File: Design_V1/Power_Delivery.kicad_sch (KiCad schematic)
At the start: 1 part

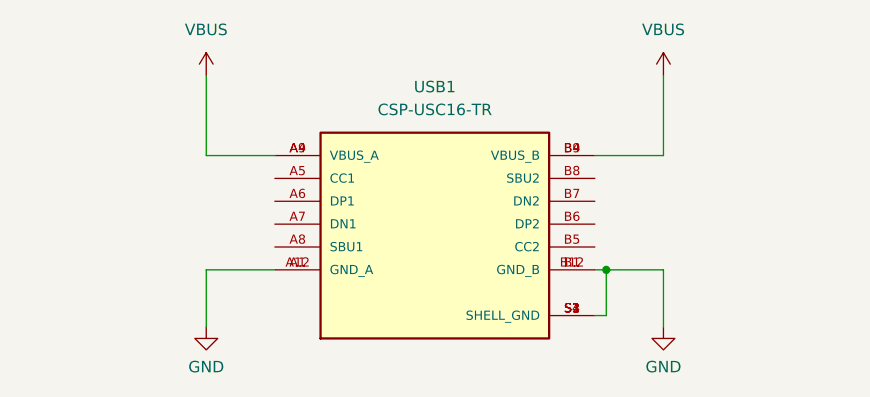
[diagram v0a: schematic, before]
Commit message: Updated Project. Added testpoints, crystal and jumpers. Added Power block
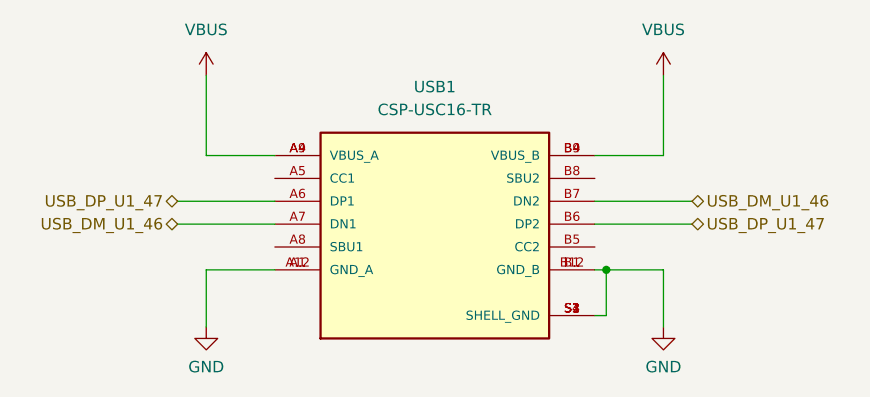
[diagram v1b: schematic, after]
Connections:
- net USB_DP_U1_47: now reaches USB1.A6 (DP1)
- net USB_DP_U1_47: now also USB1.B6 (DP2)
- net USB_DM_U1_46: now reaches USB1.A7 (DN1)
- net USB_DM_U1_46: now also USB1.B7 (DN2)
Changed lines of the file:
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@@
+    (stroke (width 0) (type default) (color 0 0 0 0))
+  )
+  (wire (pts (xy 246.38 110.49) (xy 257.175 110.49))
     (stroke (width 0) (type default) (color 0 0 0 0))
   )
   (wire (pts (xy 254 102.87) (xy 254 93.98))
+    (stroke (width 0) (type default) (color 0 0 0 0))
+  )
+  (wire (pts (xy 210.82 107.95) (xy 200.025 107.95))
+    (stroke (width 0) (type default) (color 0 0 0 0))
+  )
+  (wire (pts (xy 210.82 110.49) (xy 200.025 110.49))
+    (stroke (width 0) (type default) (color 0 0 0 0))
+  )
+  (wire (pts (xy 246.38 107.95) (xy 257.175 107.95))
     (stroke (width 0) (type default) (color 0 0 0 0))
   )
@@
     (stroke (width 0) (type default) (color 0 0 0 0))
   )
+  (hierarchical_label "USB_DP_U1_47" (shape bidirectional) (at 257.175 110.49 0)
+    (effects (font (size 1.27 1.27)) (justify left))
+  )
+  (hierarchical_label "USB_DM_U1_46" (shape bidirectional) (at 200.025 110.49 180)
+    (effects (font (size 1.27 1.27)) (justify right))
+  )
+  (hierarchical_label "USB_DP_U1_47" (shape bidirectional) (at 200.025 107.95 180)
+    (effects (font (size 1.27 1.27)) (justify right))
+  )
+  (hierarchical_label "USB_DM_U1_46" (shape bidirectional) (at 257.175 107.95 0)
+    (effects (font (size 1.27 1.27)) (justify left))
+  )
   (symbol (lib_id "power:GND") (at 203.2 121.92 0) (unit 1)
